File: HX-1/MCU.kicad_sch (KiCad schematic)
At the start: 36 parts, among them J10 Conn_01x20, J11 Conn_01x20, J3 I2C_CONN, J4 SPI_CONN, J7 FDCAN_CONN, J8 FDCAN_CONN, J9 UART_CONN, SW1 SW_SPDT, U1 STM32H723ZGT6

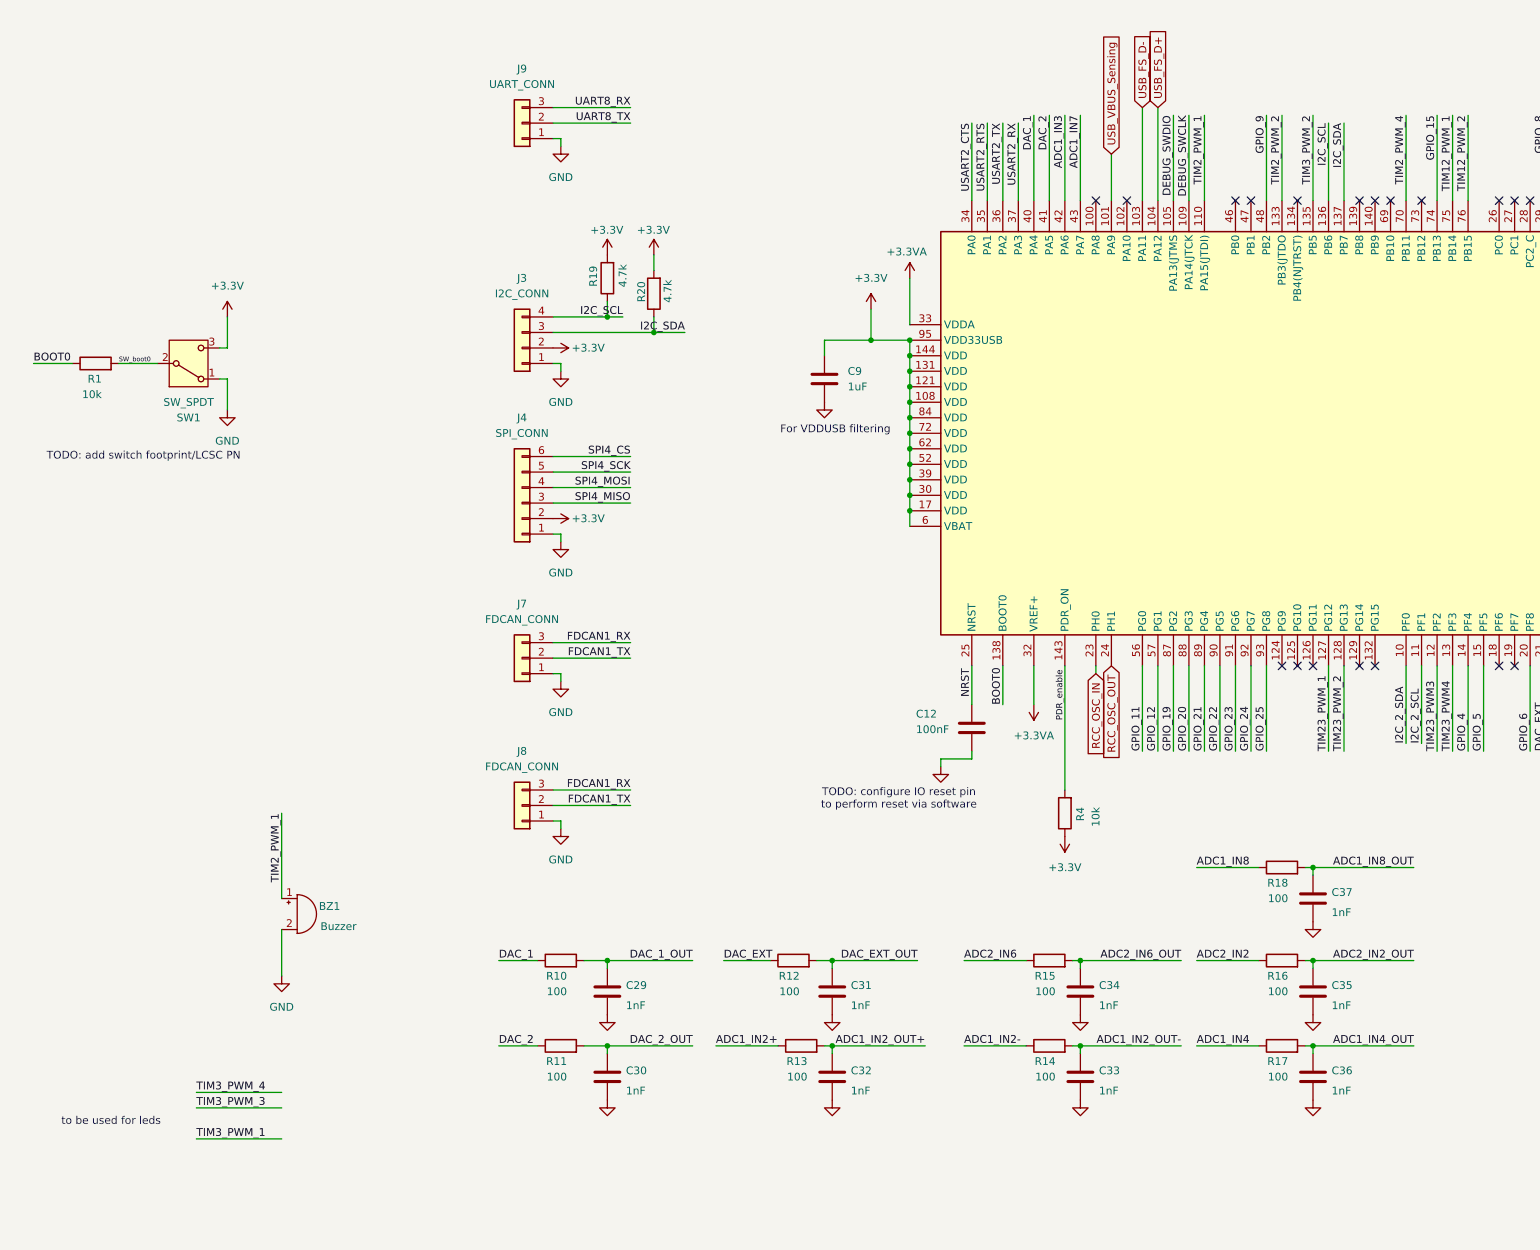
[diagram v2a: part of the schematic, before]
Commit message: add jst connectors to comms, add imu, start structuring pcb
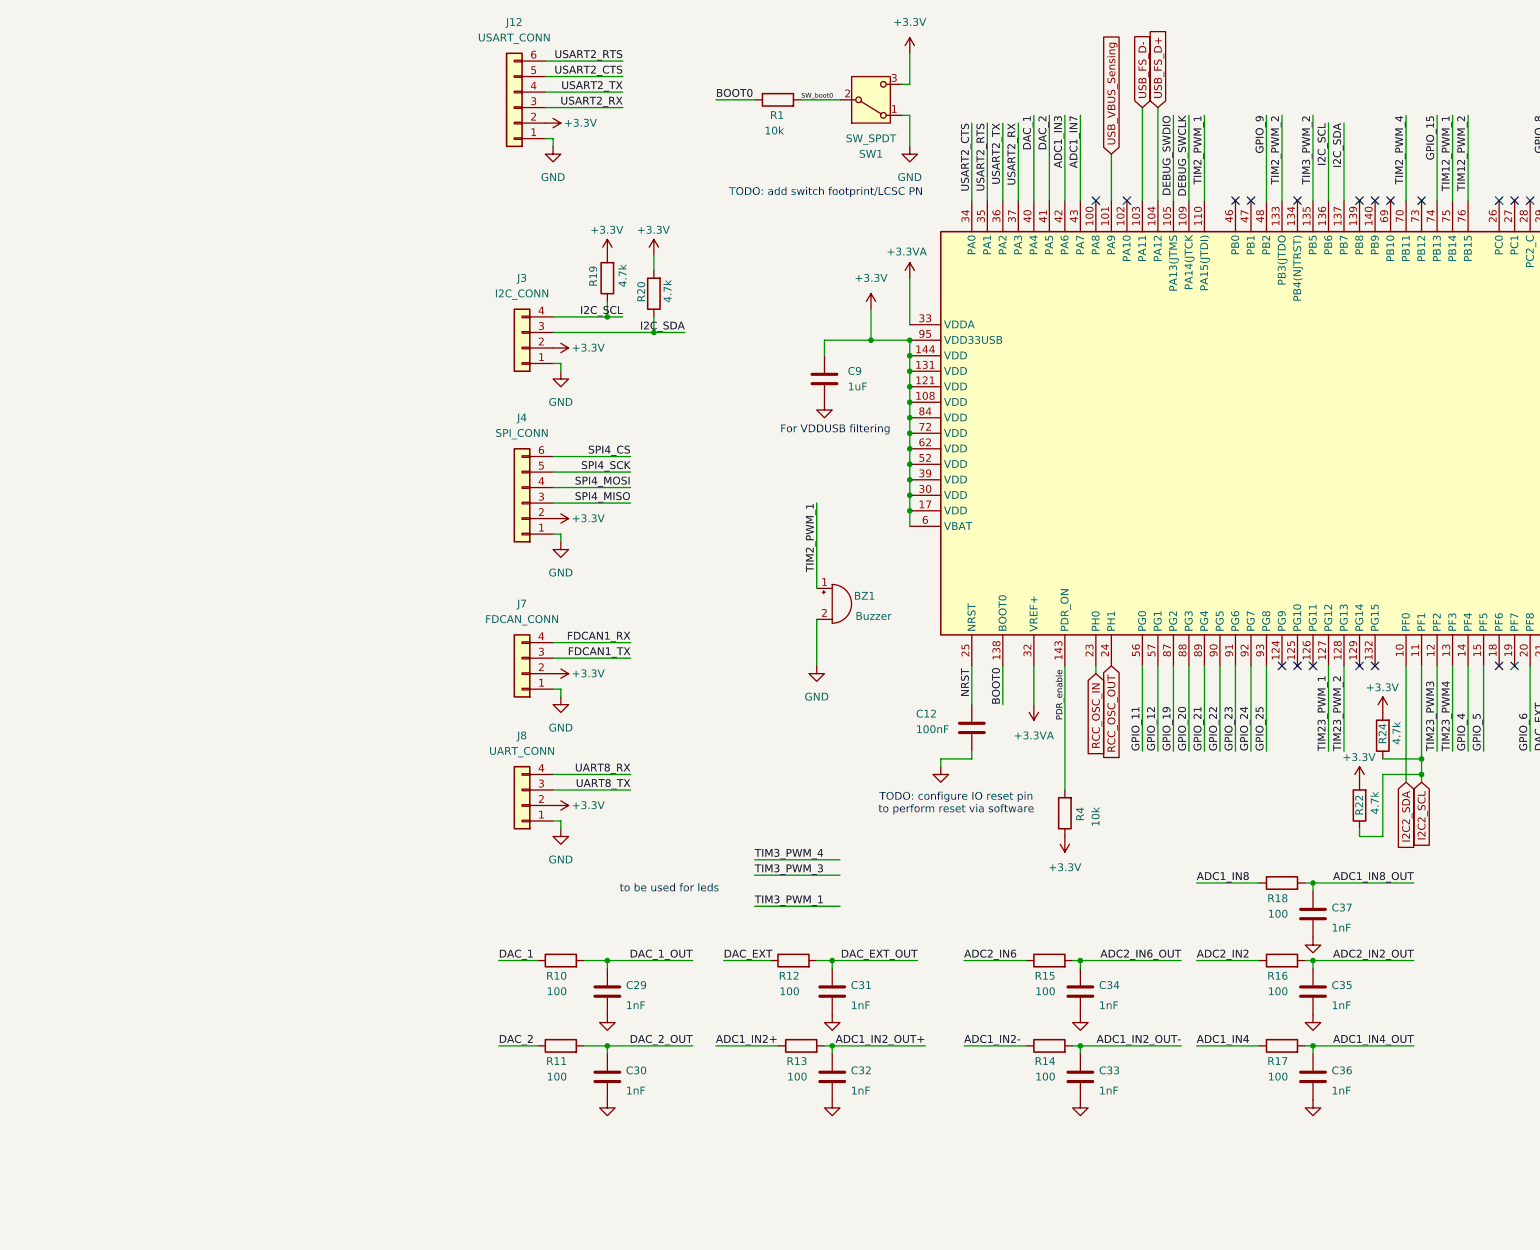
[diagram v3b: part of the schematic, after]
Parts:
- removed J7, J8: FDCAN_CONN, symbol Connector_Generic:Conn_01x03
- removed J9: UART_CONN, symbol Connector_Generic:Conn_01x03
- added J12: USART_CONN, Connector_JST:JST_PH_B4B-PH-K_1x04_P2.00mm_Vertical, symbol Connector_Generic:Conn_01x06
- added J7: FDCAN_CONN, Connector_JST:JST_PH_B4B-PH-K_1x04_P2.00mm_Vertical, symbol Connector_Generic:Conn_01x04
- added J8: UART_CONN, Connector_JST:JST_PH_B4B-PH-K_1x04_P2.00mm_Vertical, symbol Connector_Generic:Conn_01x04
- added R22, R24: 4.7k, Resistor_SMD:R_0402_1005Metric, symbol Device:R
- J3, J4: footprint (none) -> Connector_JST:JST_PH_B4B-PH-K_1x04_P2.00mm_Vertical
- R19, R20: footprint Resistor_SMD:R_0603_1608Metric -> Resistor_SMD:R_0402_1005Metric; LCSC PN (none) -> C25900
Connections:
- net +3.3V: now also J12.2 (Pin_2), J7.2 (Pin_2), J8.2 (Pin_2), R22.2, R24.2
- net FDCAN1_RX: now also J7.4 (Pin_4)
- net FDCAN1_TX: now also J7.3 (Pin_3)
- net GND: now also J12.1 (Pin_1), J7.1 (Pin_1), J8.1 (Pin_1)
- net UART8_RX: now also J8.4 (Pin_4)
- net UART8_TX: now also J8.3 (Pin_3)
- net USART2_CTS: now also J12.5 (Pin_5)
- net USART2_RTS: now also J12.6 (Pin_6)
- net USART2_RX: now also J12.3 (Pin_3)
- net USART2_TX: now also J12.4 (Pin_4)
- net I2C_2_SCL renamed I2C2_SCL
- net I2C2_SCL: now also R22.1, R24.1
- net I2C_2_SDA renamed I2C2_SDA
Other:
- moved on the sheet: BZ1, C37, R1, R18, SW1

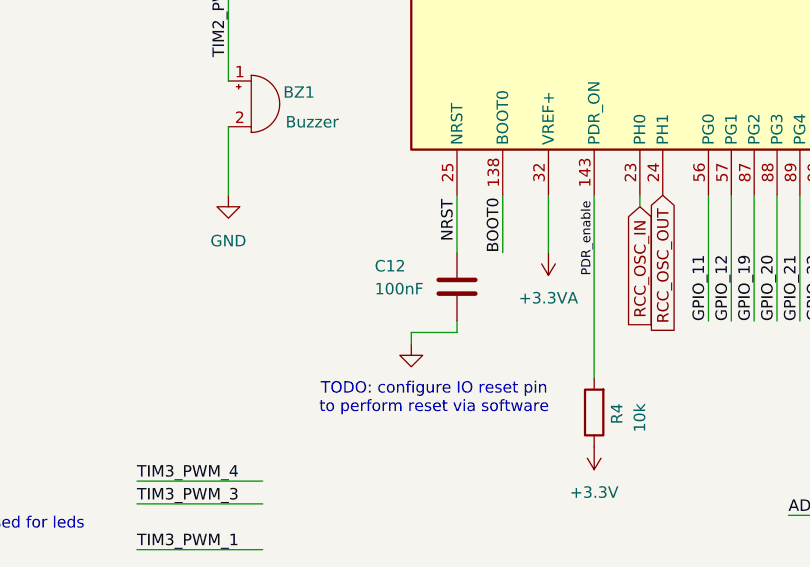
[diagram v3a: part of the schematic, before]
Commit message: change most passive components to 0402 to save space
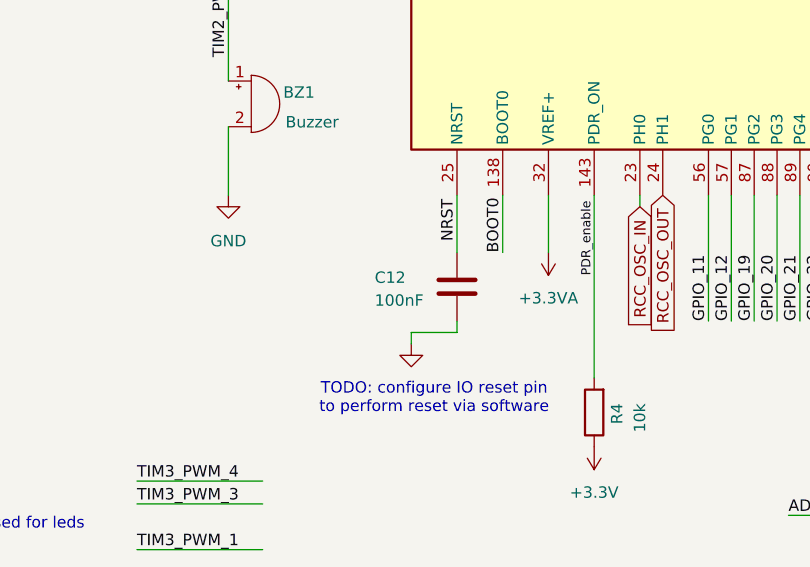
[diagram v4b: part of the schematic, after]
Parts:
- C12: footprint Capacitor_SMD:C_0603_1608Metric -> Capacitor_SMD:C_0402_1005Metric; LCSC PN C14663 -> C1525
- R1, R4: footprint Resistor_SMD:R_0603_1608Metric -> Resistor_SMD:R_0402_1005Metric; LCSC PN C25804 -> C25744

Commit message: draft board size
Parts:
- J12, J4: footprint Connector_JST:JST_PH_B4B-PH-K_1x04_P2.00mm_Vertical -> Connector_JST:JST_PH_B6B-PH-K_1x06_P2.00mm_Vertical

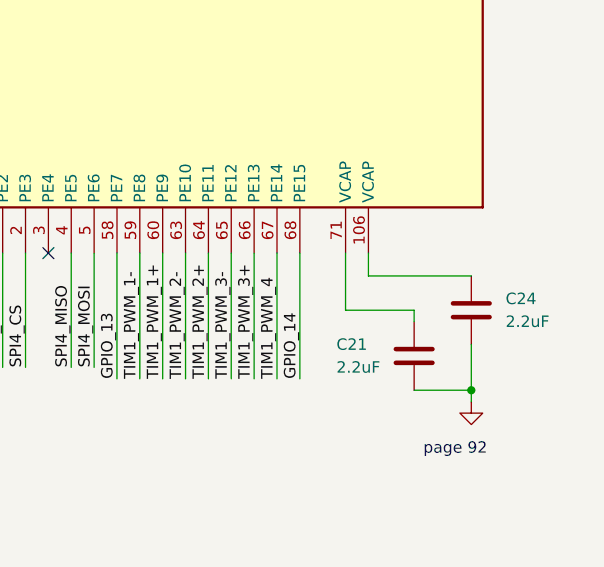
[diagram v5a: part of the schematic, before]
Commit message: change analog resistors to 0402 to make routing easier
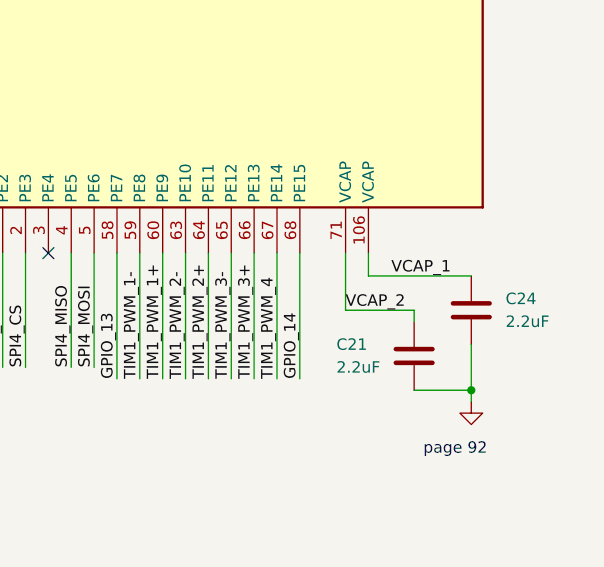
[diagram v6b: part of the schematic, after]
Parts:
- R10, R11, R12, R13, R14, R15, R16, R17, R18: footprint Resistor_SMD:R_0603_1608Metric -> Resistor_SMD:R_0402_1005Metric; LCSC PN (none) -> C25076
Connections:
- net VCAP_1: now reaches C24.1, U1.106 (VCAP)
- net VCAP_2: now reaches C21.1, U1.71 (VCAP)

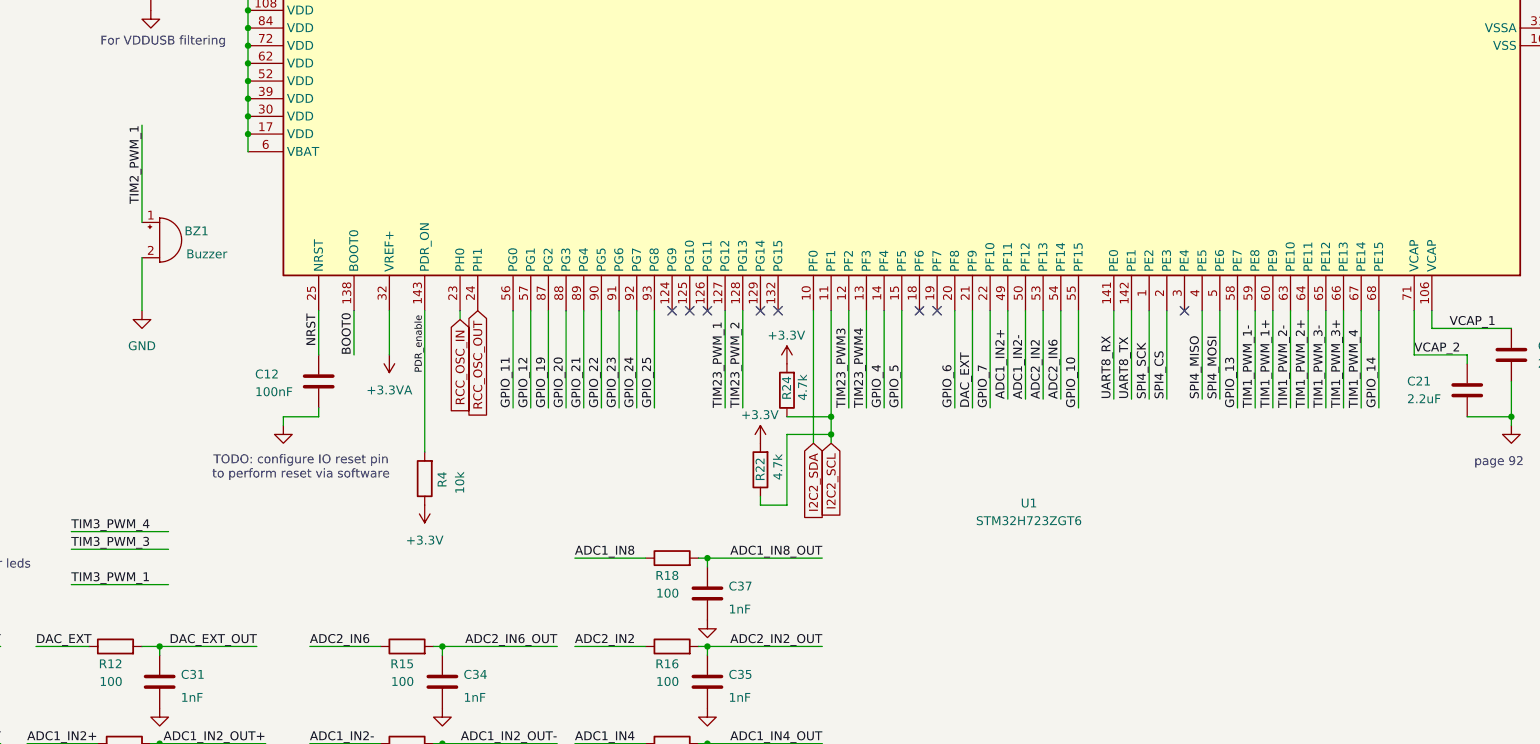
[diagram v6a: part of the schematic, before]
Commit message: update scripts to export pcb svg
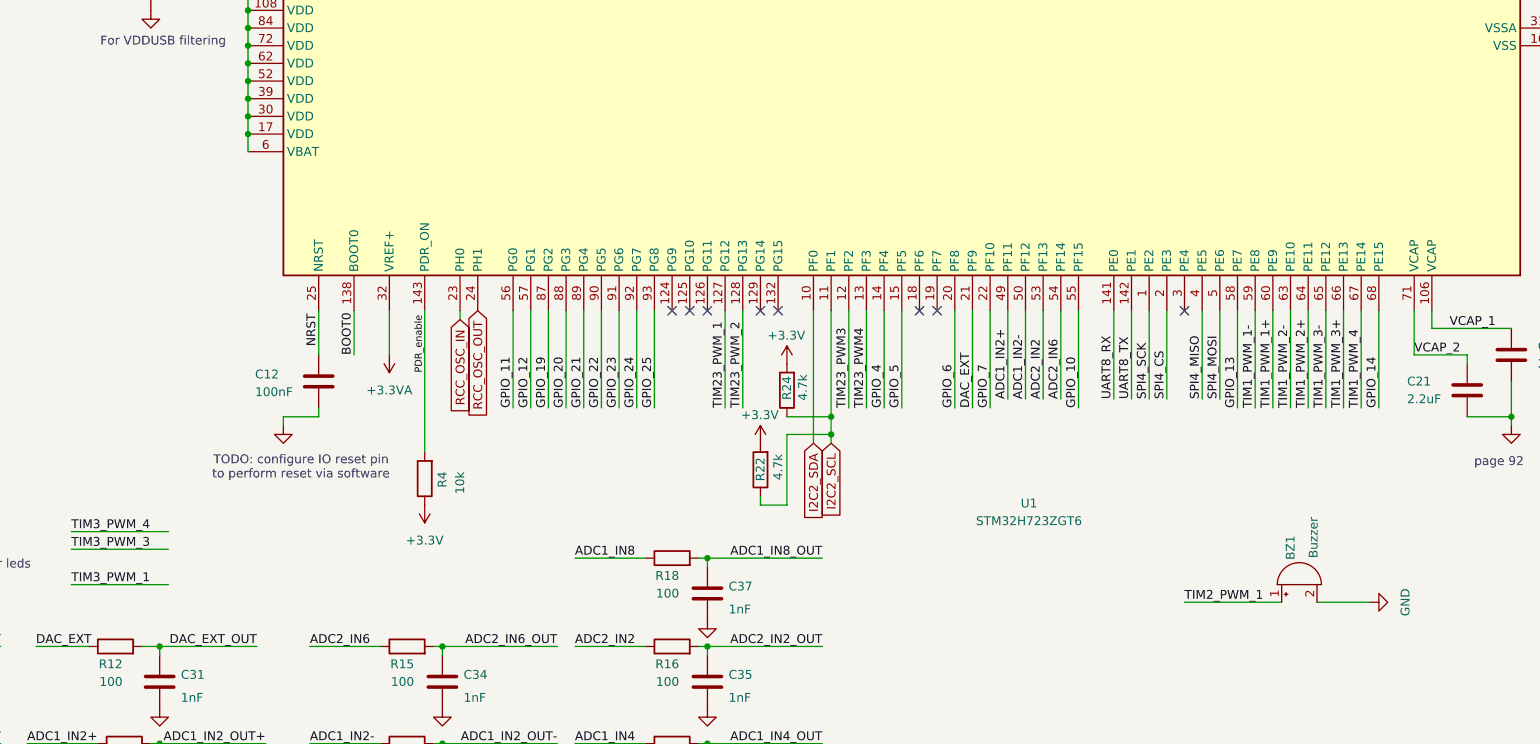
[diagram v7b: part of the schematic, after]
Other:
- moved on the sheet: BZ1

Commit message: add switch footprint
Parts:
- SW1: footprint (none) -> Switch:SW-TH_G-SWITCH_SS-12F20-G070; LCSC PN (none) -> C2848914
